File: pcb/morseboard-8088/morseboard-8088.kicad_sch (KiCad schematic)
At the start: 64 parts, among them J1 USB_B, J2 UART1, J3 TxD, J4 ~{CTS}, J5 RxD, J6 ~{RTS}, SW1 SW_SPDT, SW2 INTPORT, SW4 NMI, SW6 RESET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

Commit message: Creating new prototype
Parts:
- removed J3: TxD, Connector_PinHeader_2.54mm:PinHeader_1x03_P2.54mm_Vertical, symbol Connector:Conn_01x03_Pin
- removed J4: ~{CTS}, Connector_PinHeader_2.54mm:PinHeader_1x03_P2.54mm_Vertical, symbol Connector:Conn_01x03_Pin
- removed J5: RxD, Connector_PinHeader_2.54mm:PinHeader_1x03_P2.54mm_Vertical, symbol Connector:Conn_01x03_Pin
- removed J6: ~{RTS}, Connector_PinHeader_2.54mm:PinHeader_1x03_P2.54mm_Vertical, symbol Connector:Conn_01x03_Pin
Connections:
- net R1IN is gone; now on net UART3: U13.13 (R1IN)
- net R2IN is gone; now on net UART7: U13.8 (R2IN)
- net T1OUT is gone; now on net UART2: U13.14 (T1OUT)
- net T2OUT is gone; now on net UART8: U13.7 (T2OUT)
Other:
- note added: "Do not output on ~{INTA}!"

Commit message: Fixing erroneous board layout
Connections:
- net M renamed ~{IO}/M
- net ~{M} renamed IO/~{M}
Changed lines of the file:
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@@
 		)
 	)
-	(global_label "M"
-		(shape input)
-		(at 302.26 43.18 180)
-		(fields_autoplaced yes)
-		(effects
-			(font
-				(size 1.27 1.27)
-			)
-			(justify right)
-		)
-		(property "Intersheetrefs" "${INTERSHEET_REFS}"
-			(at 297.8234 43.18 0)
-			(effects
-				(font
-					(size 1.27 1.27)
-				)
-				(justify right)
-				(hide yes)
-			)
-		)
-	)
 	(global_label "~{IO01}"
 		(shape input)
@@
 		)
 	)
-	(global_label "M"
-		(shape input)
-		(at 217.17 134.62 180)
-		(fields_autoplaced yes)
-		(effects
-			(font
-				(size 1.27 1.27)
-			)
-			(justify right)
-		)
-		(property "Intersheetrefs" "${INTERSHEET_REFS}"
-			(at 212.7334 134.62 0)
-			(effects
-				(font
-					(size 1.27 1.27)
-				)
-				(justify right)
-				(hide yes)
-			)
-		)
-	)
 	(global_label "~{INTA}"
 		(shape input)
@@
 		)
 	)
+	(global_label "~{IO}{slash}M"
+		(shape input)
+		(at 217.17 151.13 180)
+		(fields_autoplaced yes)
+		(effects
+			(font
+				(size 1.27 1.27)
+			)
+			(justify right)
+		)
+		(property "Intersheetrefs" "${INTERSHEET_REFS}"
+			(at 209.4676 151.13 0)
+			(effects
+				(font
+					(size 1.27 1.27)
+				)
+				(justify right)
+				(hide yes)
+			)
+		)
+	)
 	(global_label "D5"
 		(shape input)
@@
 		)
 	)
+	(global_label "~{IO}{slash}M"
+		(shape input)
+		(at 217.17 134.62 180)
+		(fields_autoplaced yes)
+		(effects
+			(font
+				(size 1.27 1.27)
+			)
+			(justify right)
+		)
+		(property "Intersheetrefs" "${INTERSHEET_REFS}"
+			(at 209.4676 134.62 0)
+			(effects
+				(font
+					(size 1.27 1.27)
+				)
+				(justify right)
+				(hide yes)
+			)
+		)
+	)
 	(global_label "L1"
 		(shape input)
@@
 		)
 	)
+	(global_label "IO{slash}~{M}"
+		(shape input)
+		(at 180.34 153.67 180)
+		(fields_autoplaced yes)
+		(effects
+			(font
+				(size 1.27 1.27)
+			)
+			(justify right)
+		)
+		(property "Intersheetrefs" "${INTERSHEET_REFS}"
+			(at 172.6376 153.67 0)
+			(effects
+				(font
+					(size 1.27 1.27)
+				)
+				(justify right)
+				(hide yes)
+			)
+		)
+	)
 	(global_label "UART3"
 		(shape input)
@@
 		)
 	)
+	(global_label "~{IO}{slash}M"
+		(shape input)
+		(at 302.26 43.18 180)
+		(fields_autoplaced yes)
+		(effects
+			(font
+				(size 1.27 1.27)
+			)
+			(justify right)
+		)
+		(property "Intersheetrefs" "${INTERSHEET_REFS}"
+			(at 294.5576 43.18 0)
+			(effects
+				(font
+					(size 1.27 1.27)
+				)
+				(justify right)
+				(hide yes)
+			)
+		)
+	)
 	(global_label "A1"
 		(shape input)
@@
 		)
 	)
-	(global_label "M"
-		(shape input)
-		(at 217.17 151.13 180)
-		(fields_autoplaced yes)
-		(effects
-			(font
-				(size 1.27 1.27)
-			)
-			(justify right)
-		)
-		(property "Intersheetrefs" "${INTERSHEET_REFS}"
-			(at 212.7334 151.13 0)
-			(effects
-				(font
-					(size 1.27 1.27)
-				)
-				(justify right)
-				(hide yes)
-			)
-		)
-	)
 	(global_label "A4"
 		(shape input)
@@
 		)
 	)
-	(global_label "M"
+	(global_label "~{IO}{slash}M"
 		(shape input)
 		(at 199.39 153.67 0)
@@
 		)
 		(property "Intersheetrefs" "${INTERSHEET_REFS}"
-			(at 203.8266 153.67 0)
+			(at 207.0924 153.67 0)
 			(effects
 				(font
@@
 		)
 	)
-	(global_label "~{M}"
+	(global_label "IO{slash}~{M}"
 		(shape input)
 		(at 60.96 100.33 0)
@@
 		)
 		(property "Intersheetrefs" "${INTERSHEET_REFS}"
-			(at 65.3966 100.33 0)
+			(at 68.6624 100.33 0)
 			(effects
 				(font
@@
 			(effects
 				(font
-					(size 1.27 1.27)
-				)
-				(justify right)
-				(hide yes)
-			)
-		)
-	)
-	(global_label "~{M}"
-		(shape input)
-		(at 180.34 153.67 180)
-		(fields_autoplaced yes)
-		(effects
-			(font
-				(size 1.27 1.27)
-			)
-			(justify right)
-		)
-		(property "Intersheetrefs" "${INTERSHEET_REFS}"
-			(at 175.9034 153.67 0)
-			(effects
-				(font

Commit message: Polishing schematics
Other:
- note added: "8088 CPU and latch registers"
- note added: "Clock oscillator Used for both CPU and UART"
- note added: "DIP switch interrupt vector"
- note added: "Decoupling caps"
- note added: "Glue logic"
- note added: "Port 0x00 LED latch"
- note added: "Power and reset circuitry"
- note added: "ROM and RAM (2 x 512 KiB)"
- note added: "UART"
- moved on the sheet: C1, C10, C11, C12, C13, C14, C15, C16, C17, C18, C19, C2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

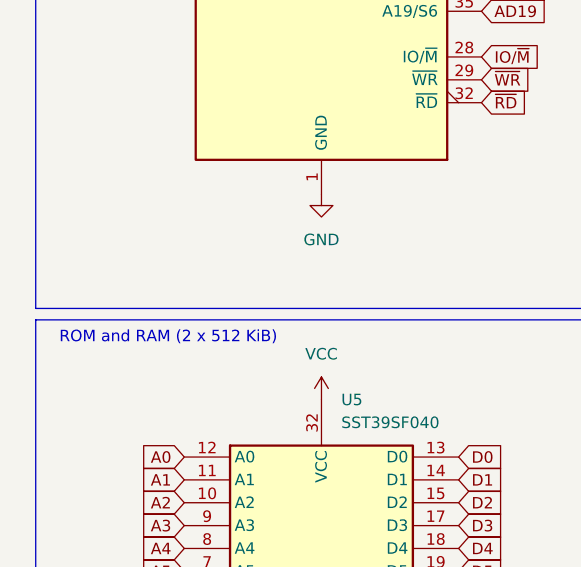
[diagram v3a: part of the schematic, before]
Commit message: Removing 8087 based board
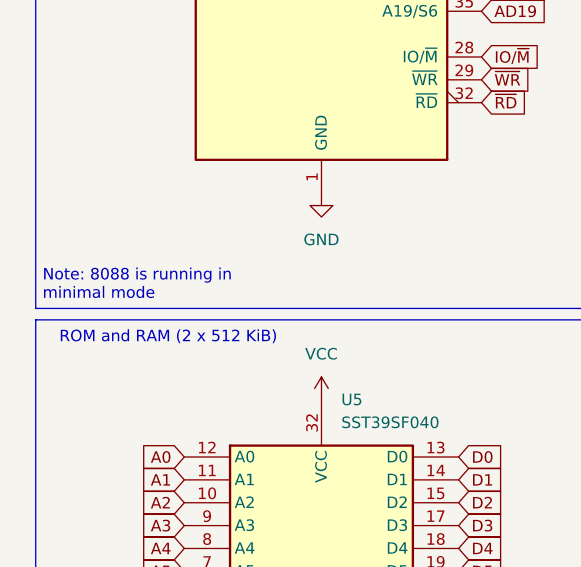
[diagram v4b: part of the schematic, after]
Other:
- note added: "Note: 8088 is running in minimal mode"
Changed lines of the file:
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@@
+		)
+	)
+	(text "Note: 8088 is running in\nminimal mode"
+		(exclude_from_sim no)
+		(at 14.732 125.73 0)
+		(effects
+			(font
+				(size 1.27 1.27)
+			)
+			(justify left)
 		)
 	)
